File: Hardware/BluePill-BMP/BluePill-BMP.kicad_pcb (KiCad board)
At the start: 2 copper layers, 70 x 60 mm, 18 parts, among them J1 SWO, J2 JTAG, J3 GDB_COMM, J4 VCC, J5 GND, J6 LogicAna, U1 FT232RL_Breakout, U2 STM32F103 BluePill

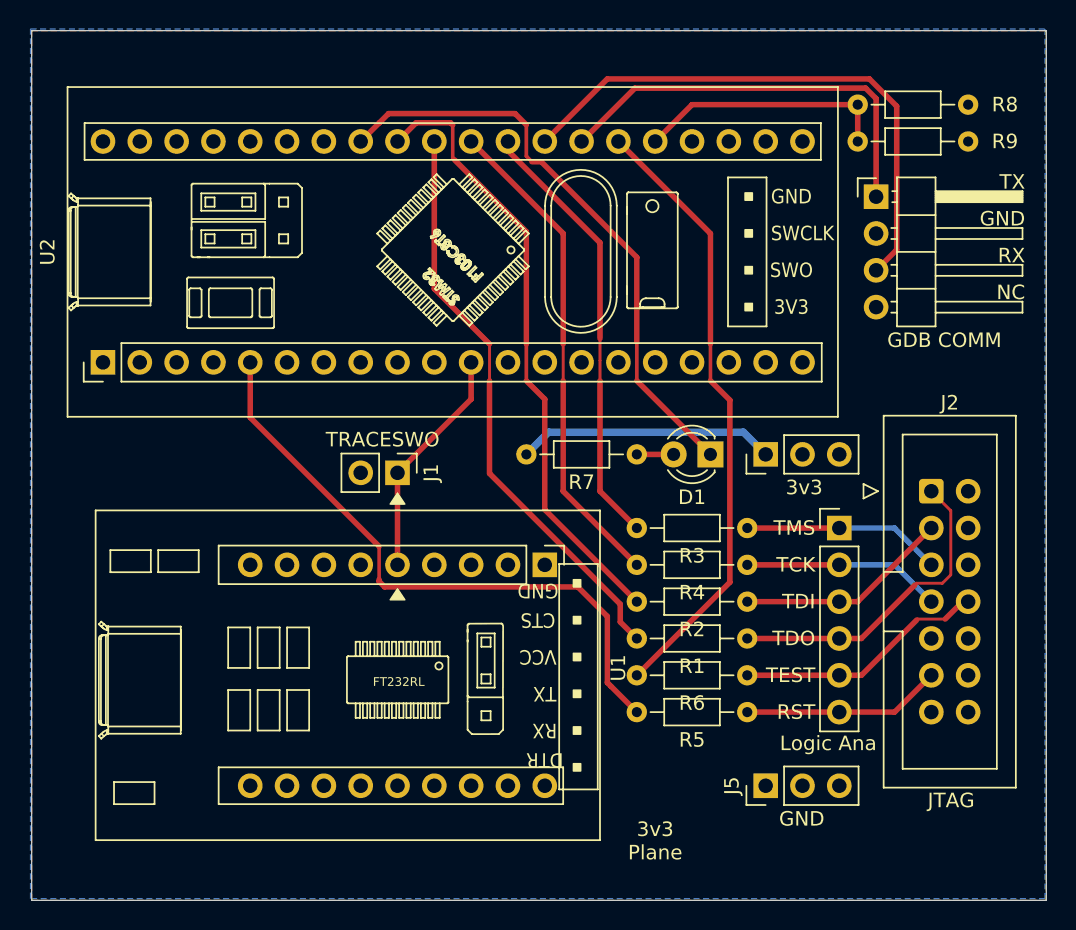
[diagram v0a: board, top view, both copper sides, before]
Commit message: - JTAG over SPI
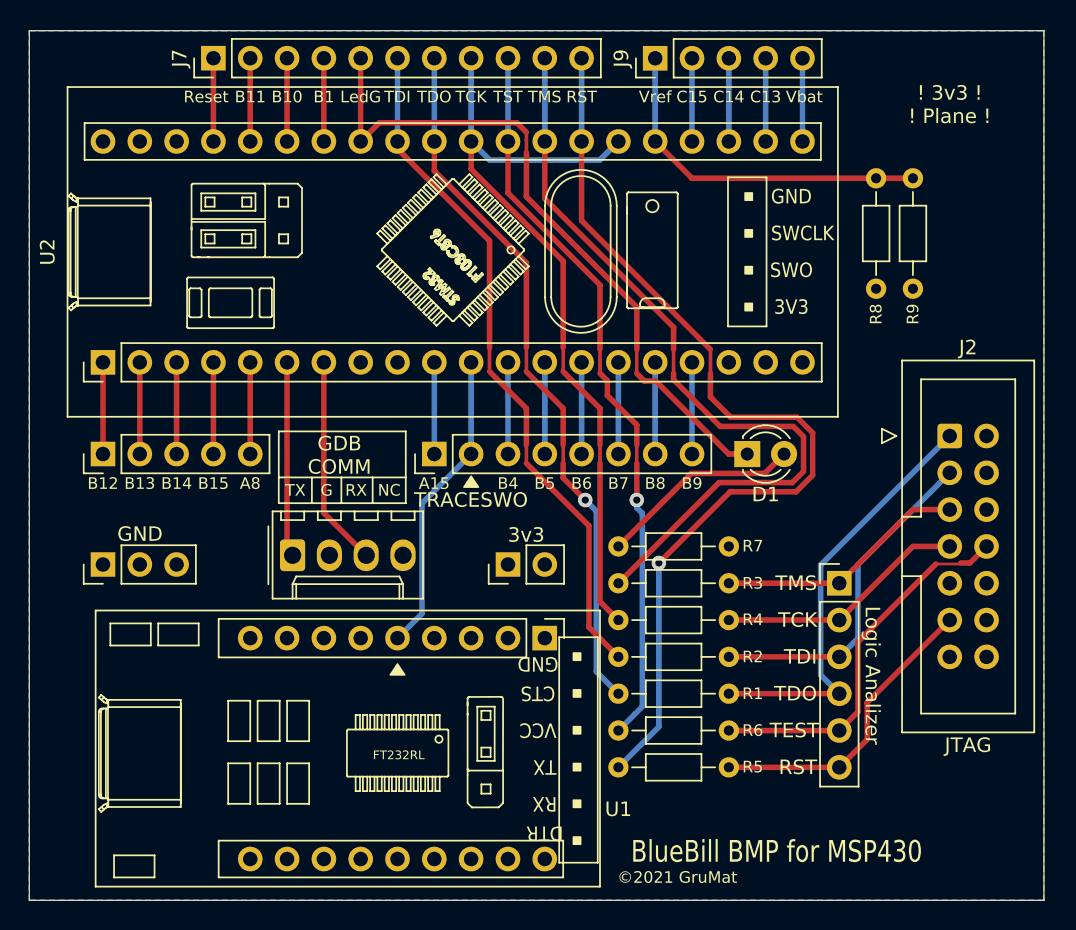
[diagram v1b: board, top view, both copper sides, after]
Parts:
- added J7: Conn_01x11, Connector_PinHeader_2.54mm:PinHeader_1x11_P2.54mm_Vertical, F.Cu at (129.5, 66.9)
- added J8: Conn_01x05, Connector_PinHeader_2.54mm:PinHeader_1x05_P2.54mm_Vertical, F.Cu at (121.9, 94.2)
- added J9: Conn_01x05, Connector_PinHeader_2.54mm:PinHeader_1x05_P2.54mm_Vertical, F.Cu at (160.0, 66.9)
- J1: value SWO -> Conn_01x08; footprint Connector_PinHeader_2.54mm:PinHeader_1x02_P2.54mm_Vertical -> Connector_PinHeader_2.54mm:PinHeader_1x08_P2.54mm_Vertical
- J3: footprint Connector_PinHeader_2.54mm:PinHeader_1x04_P2.54mm_Horizontal -> Connector_Molex:Molex_KK-254_AE-6410-04A_1x04_P2.54mm_Vertical
- J4: footprint Connector_PinHeader_2.54mm:PinHeader_1x03_P2.54mm_Vertical -> Connector_PinHeader_2.54mm:PinHeader_1x02_P2.54mm_Vertical
- moved J5 48.2 mm to (121.9, 101.8)
- moved J3 47.3 mm to (135.0, 101.2)
- moved J4 19.3 mm to (149.9, 101.8)
- moved R9 10.9 mm to (177.8, 82.8), turned to 90 degrees
- moved R7 6.48 mm to (157.5, 100.6), turned to 0 degrees
- moved R8 5.24 mm to (175.3, 75.2), turned to 270 degrees
- moved U1 5.06 mm to (152.4, 106.9)
- moved J2 4.02 mm to (180.3, 93.0)
- moved R1 4.02 mm to (165.1, 110.7)
- moved R3 4.02 mm to (165.1, 103.1)
- moved R4 4.02 mm to (165.1, 105.7)
- moved R5 4.02 mm to (165.1, 115.8)
- moved R6 4.02 mm to (165.1, 113.3)
- moved R2 4.02 mm to (165.1, 108.2)
- moved J6 3.81 mm to (172.7, 103.1)
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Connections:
- J1 pad 1: /TRACESWO -> /PA15
- J1 pad 2: GND -> /TRACESWO
- U2 pad 1: Net-(U2-Pad1) -> /PB12
- U2 pad 10: Net-(U2-Pad10) -> /PA15
- U2 pad 12: Net-(U2-Pad12) -> /PB4
- U2 pad 13: Net-(U2-Pad13) -> /PB5
- U2 pad 14: Net-(U2-Pad14) -> /PB6
- U2 pad 15: Net-(U2-Pad15) -> /PB7
- U2 pad 16: Net-(U2-Pad16) -> /PB8
- U2 pad 17: Net-(U2-Pad17) -> /PB9
- U2 pad 2: Net-(U2-Pad2) -> /PB13
- U2 pad 21: Net-(U2-Pad21) -> /VBAT
- U2 pad 22: Net-(U2-Pad22) -> /PC13
- U2 pad 23: Net-(U2-Pad23) -> /PC14
- U2 pad 24: Net-(U2-Pad24) -> /PC15
- U2 pad 26: /BTEST -> /BTCK
- U2 pad 27: /GDB_TX -> /BRST
- U2 pad 28: /GDB_RX -> /BTMS
- U2 pad 29: /BTMS -> /BTEST
- U2 pad 3: Net-(U2-Pad3) -> /PB14
- U2 pad 34: Net-(U2-Pad34) -> /PB1
- U2 pad 35: Net-(U2-Pad35) -> /PB10
- U2 pad 36: Net-(U2-Pad36) -> /PB11
- U2 pad 37: Net-(U2-Pad37) -> /RST
- U2 pad 4: Net-(U2-Pad4) -> /PB15
- U2 pad 5: /BRST -> /PA8
- U2 pad 6: Net-(U2-Pad6) -> /GDB_TX
- U2 pad 7: Net-(U2-Pad7) -> /GDB_RX
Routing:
- net /BTMS: track 30.4 -> 54.8 mm
- net /GDB_RX: track 38.8 -> 14.5 mm
- net /BRST: track 43.0 -> 66.4 mm, vias 0 -> 1
- net /BTCK: track 33.9 -> 54.2 mm
- net +3V3: track 17.8 -> 0.00 mm
- net /GDB_TX: track 28.9 -> 13.5 mm
- net Net-(D1-Pad2): track 2.54 -> 14.1 mm
- net /BTDO: track 40.1 -> 49.1 mm, vias 0 -> 1
- net /JTDI: track 14.8 -> 23.5 mm
- net /JTEST: track 17.3 -> 25.9 mm
- net /BTEST: track 42.7 -> 50.9 mm, vias 0 -> 1
- net /JTDO: track 22.2 -> 29.6 mm
- net /JRST: track 13.8 -> 20.9 mm
- net /VREF: track 17.6 -> 24.6 mm
- net /LEDG: track 40.9 -> 47.7 mm
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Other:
- board text added: "! 3v3 ! ! Plane !"
- board text added: "A15"
- board text added: "A8"
- board text added: "B1"
- board text added: "B10"
- board text added: "B11"
- board text added: "B12"
- board text added: "B13"
- board text added: "B14"
- board text added: "B15"
- board text added: "B4"
- board text added: "B5"
- board text added: "B6"
- board text added: "B7"
- board text added: "B8"
- board text added: "B9"
- board text added: "BlueBill BMP for MSP430"
- board text added: "C13"
- board text added: "C14"
- board text added: "C15"
- board text added: "G"
- board text added: "LedG"
- board text added: "Logic Analizer"
- board text added: "Reset"
- board text added: "TST"
- board text added: "Vbat"
- board text added: "Vref"
- board text added: "©2021 GruMat"
- board text removed: "3v3 Plane"
- board text removed: "Logic Ana"

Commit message: Updated Hardware Schematics and Boards
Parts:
- removed J9: Conn_01x05, Connector_PinHeader_2.54mm:PinHeader_1x05_P2.54mm_Vertical
- removed the R1 at (165.1, 110.7)
- added C1: 100nF, Capacitor_THT:C_Disc_D4.3mm_W1.9mm_P5.00mm, F.Cu at (182.9, 85.3)
- added R10: 330, Resistor_THT:R_Axial_DIN0204_L3.6mm_D1.6mm_P7.62mm_Horizontal, F.Cu at (157.5, 115.8)
- added R11: 330, Resistor_THT:R_Axial_DIN0204_L3.6mm_D1.6mm_P7.62mm_Horizontal, F.Cu at (165.1, 110.7)
- added R9: 330, Resistor_THT:R_Axial_DIN0204_L3.6mm_D1.6mm_P7.62mm_Horizontal, F.Cu at (157.5, 118.3)
- J1: value Conn_01x08 -> Conn_01x07; footprint Connector_PinHeader_2.54mm:PinHeader_1x08_P2.54mm_Vertical -> Connector_PinHeader_2.54mm:PinHeader_1x07_P2.54mm_Vertical
- J3: renamed from J7; footprint Connector_PinHeader_2.54mm:PinHeader_1x11_P2.54mm_Vertical -> Connector_PinHeader_2.54mm:PinHeader_1x13_P2.54mm_Vertical
- J8: renamed from J6; footprint Connector_PinHeader_2.54mm:PinHeader_1x06_P2.54mm_Vertical -> Connector_PinHeader_2.54mm:PinHeader_1x07_P2.54mm_Vertical
- moved J3 33.0 mm to (162.6, 66.9), turned to 270 degrees
- moved R8 5.10 mm to (165.1, 108.2)
- moved R1 2.56 mm to (157.5, 98.0)
- moved R6 2.56 mm to (165.1, 103.1)
- moved R4 2.56 mm to (165.1, 105.6)
- moved R5 2.56 mm to (165.1, 100.6)
- moved R7 2.56 mm to (165.1, 113.3)
- moved J1 2.54 mm to (147.3, 94.2)
- renumbered J8 to J2, J3 to J4, J4 to J5, J5 to J6, J2 to J7, R7 to R1, R8 to R2, R9 to R3, R2 to R4, R3 to R5, R4 to R6, R5 to R7, R6 to R8
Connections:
- J1 pad 1: /PA15 -> /TRACESWO
- J1 pad 2: /TRACESWO -> Net-(J1-Pad2)
- J1 pad 3: /PB4 -> /PB5
- J1 pad 4: /PB5 -> /BTCK
- J1 pad 5: /PB6 -> /BTMS
- J1 pad 6: /PB7 -> /PB8
- J1 pad 7: /PB8 -> /PB9
- J2 pad 1: /PB12 -> /BRST
- J2 pad 2: /PB13 -> /BTCK
- J2 pad 3: /PB14 -> /JTDO
- J2 pad 4: /PB15 -> /BTDI
- J2 pad 5: /PA8 -> /BTEST
- J3 pad 1: /RST -> /PC13
- J3 pad 10: /BTMS -> /LEDG
- J3 pad 11: /BRST -> /PB1
- J3 pad 2: /PB11 -> /VREF
- J3 pad 3: /PB10 -> /PA1
- J3 pad 4: /PB1 -> /PA2
- J3 pad 5: /LEDG -> /PA3
- J3 pad 6: /BTDI -> /PA4
- J3 pad 7: /BTDO -> /PA5
- J3 pad 8: /BTCK -> /PA6
- J3 pad 9: /BTEST -> /PA7
- J7 pad 12: Net-(J2-Pad12) -> /JTXD
- J7 pad 13: Net-(J2-Pad13) -> GND
- J7 pad 14: Net-(J2-Pad14) -> /JRXD
- U2 pad 1: /PB12 -> /BRST
- U2 pad 10: /PA15 -> Net-(U2-Pad10)
- U2 pad 12: /PB4 -> Net-(U2-Pad12)
- U2 pad 14: /PB6 -> /BTCK
- U2 pad 15: /PB7 -> /BTMS
- U2 pad 2: /PB13 -> /BTCK
- U2 pad 21: /VBAT -> Net-(U2-Pad21)
- U2 pad 23: /PC14 -> Net-(U2-Pad23)
- U2 pad 24: /PC15 -> Net-(U2-Pad24)
- U2 pad 26: /BTCK -> /PA1
- U2 pad 27: /BRST -> /PA2
- U2 pad 28: /BTMS -> /PA3
- U2 pad 29: /BTEST -> /PA4
- U2 pad 3: /PB14 -> /JTDO
- U2 pad 30: /BTCK -> /PA5
- U2 pad 31: /BTDO -> /PA6
- U2 pad 32: /BTDI -> /PA7
- U2 pad 35: /PB10 -> /BTXD
- U2 pad 36: /PB11 -> /BRXD
- U2 pad 37: /RST -> Net-(U2-Pad37)
- U2 pad 4: /PB15 -> /BTDI
- U2 pad 5: /PA8 -> /BTEST
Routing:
- net +3V3: track 0.00 -> 112.2 mm
- net /BRXD: track 0.00 -> 98.9 mm
- net /BTXD: track 0.00 -> 94.2 mm
- net /JTDO: track 29.6 -> 89.7 mm
- net /BTDO: track 49.1 -> 0.00 mm, vias 1 -> 0
- net /BTMS: track 54.8 -> 15.2 mm
- net /JTXD: track 0.00 -> 31.7 mm
- net /JRXD: track 0.00 -> 27.5 mm
- net /BRST: track 66.4 -> 56.7 mm, vias 1 -> 0
- net /BTDI: track 47.6 -> 55.9 mm
- net /PA6: track 0.00 -> 7.32 mm
- net /PA5: track 0.00 -> 7.32 mm
- net /PA3: track 0.00 -> 7.32 mm
- net /PA2: track 0.00 -> 7.32 mm
- net GND: track 0.00 -> 6.95 mm, vias 0 -> 14
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- added copper zone on F.Cu, net GND
- removed copper zone on F.Cu, net +3V3
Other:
- board text added: "A1"
- board text added: "A2"
- board text added: "A3"
- board text added: "A4"
- board text added: "A5"
- board text added: "A6"
- board text added: "A7"
- board text added: "BRX"
- board text added: "BTX"
- board text added: "JTAG MSP430"
- board text added: "©2021 by GruMat github.com/grumat/black-magic-probe-msp430"
- board text removed: "! 3v3 ! ! Plane !"
- board text removed: "A15"
- board text removed: "A8"
- board text removed: "B10"
- board text removed: "B11"
- board text removed: "B12"
- board text removed: "B13"
- board text removed: "B14"
- board text removed: "B15"
- board text removed: "B4"
- board text removed: "B6"
- board text removed: "B7"
- board text removed: "C14"
- board text removed: "C15"
- board text removed: "JTAG"
- board text removed: "Reset"
- board text removed: "Vbat"
- board text removed: "©2021 GruMat"

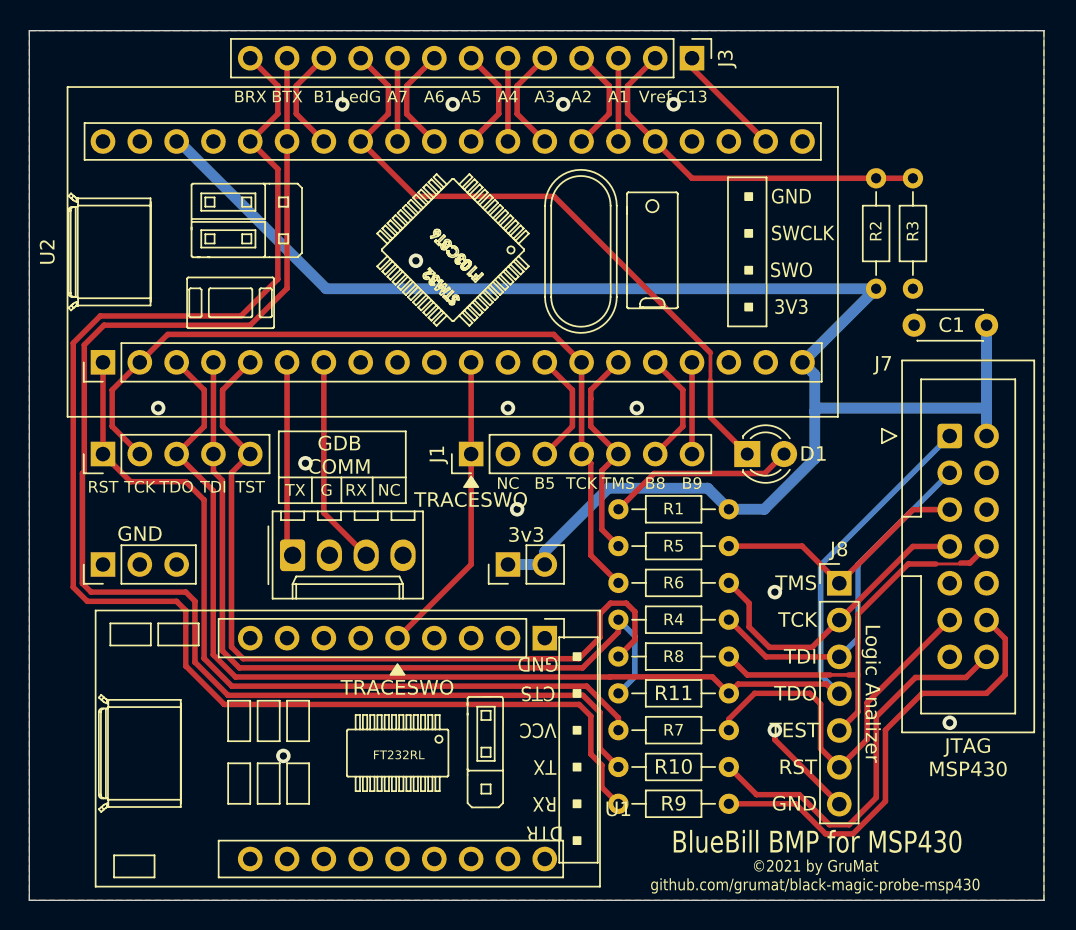
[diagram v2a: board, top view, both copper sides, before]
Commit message: Revised BluePill Prototype board
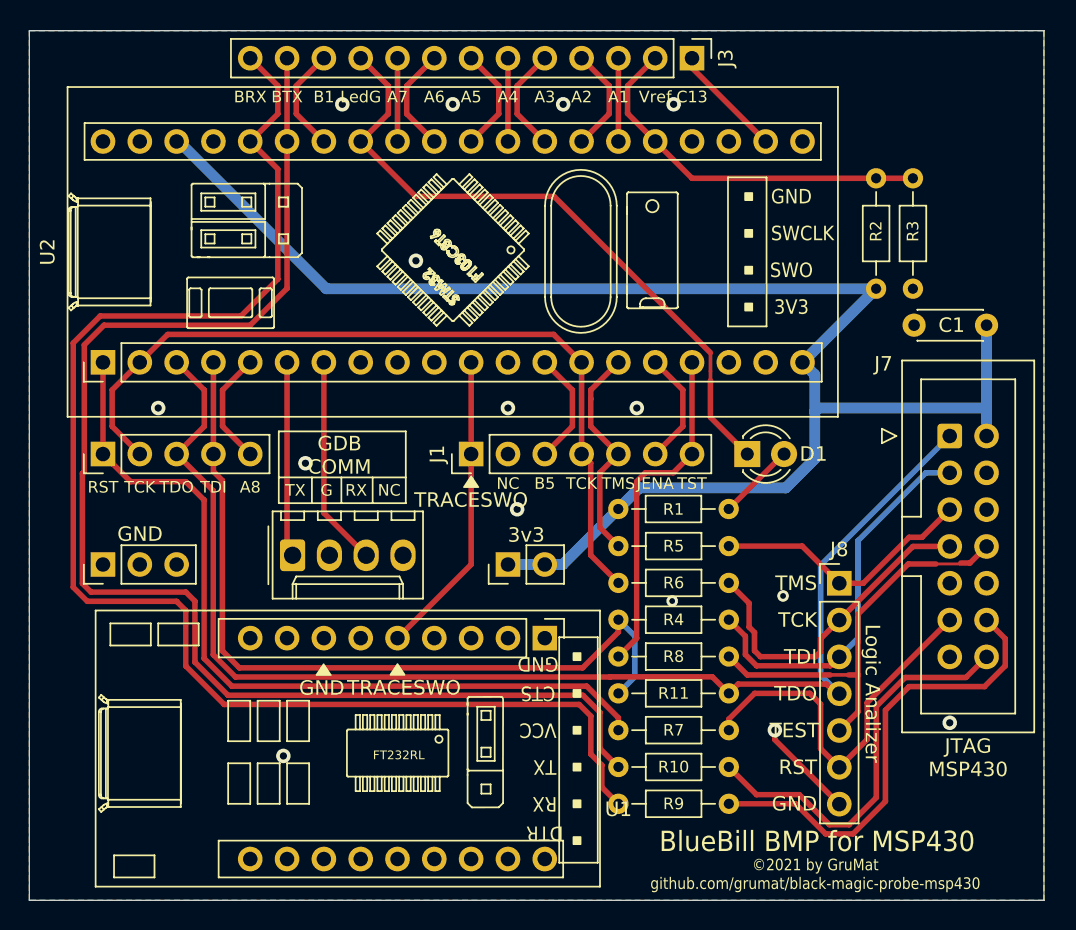
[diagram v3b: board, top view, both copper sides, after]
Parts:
- moved R1 7.61 mm to (165.1, 98.0), turned to 180 degrees
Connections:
- net /PB8 renamed /JENA
- J1 pad 7: /PB9 -> /BTEST
- J2 pad 5: /BTEST -> /PA8
- U2 pad 17: /PB9 -> /BTEST
- U2 pad 5: /BTEST -> /PA8
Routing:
- net /BTEST: track 56.3 -> 23.5 mm
- net /PA8: track 0.00 -> 7.91 mm
- net Net-(D1-Pad2): track 13.0 -> 5.39 mm
- net /PB9: track 6.33 -> 0.00 mm
- net /JTDI: track 24.5 -> 26.8 mm
- net /JTCK: track 20.9 -> 22.7 mm
- net +3V3: track 112.2 -> 110.4 mm
- net GND: vias 14 -> 15
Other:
- board text added: "A8"
- board text added: "JENA"
- board text removed: "B8"
- board text removed: "B9"

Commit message: KiCad6 evaluation
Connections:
- J1 pad 2: Net-(J1-Pad2) -> unconnected-(J1-Pad2)
- J4 pad 4: Net-(J4-Pad4) -> unconnected-(J4-Pad4)
- J7 pad 10: Net-(J7-Pad10) -> unconnected-(J7-Pad10)
- J7 pad 4: Net-(J7-Pad4) -> unconnected-(J7-Pad4)
- J7 pad 6: Net-(J7-Pad6) -> unconnected-(J7-Pad6)
- U1 pad 1: Net-(U1-Pad1) -> unconnected-(U1-Pad1)
- U1 pad 10: Net-(U1-Pad10) -> unconnected-(U1-Pad10)
- U1 pad 11: Net-(U1-Pad11) -> unconnected-(U1-Pad11)
- U1 pad 12: Net-(U1-Pad12) -> unconnected-(U1-Pad12)
- U1 pad 13: Net-(U1-Pad13) -> unconnected-(U1-Pad13)
- U1 pad 14: Net-(U1-Pad14) -> unconnected-(U1-Pad14)
- U1 pad 15: Net-(U1-Pad15) -> unconnected-(U1-Pad15)
- U1 pad 16: Net-(U1-Pad16) -> unconnected-(U1-Pad16)
- U1 pad 17: Net-(U1-Pad17) -> unconnected-(U1-Pad17)
- U1 pad 18: Net-(U1-Pad18) -> unconnected-(U1-Pad18)
- U1 pad 2: Net-(U1-Pad2) -> unconnected-(U1-Pad2)
- U1 pad 3: Net-(U1-Pad3) -> unconnected-(U1-Pad3)
- U1 pad 4: Net-(U1-Pad4) -> unconnected-(U1-Pad4)
- U1 pad 6: Net-(U1-Pad6) -> unconnected-(U1-Pad6)
- U1 pad 8: Net-(U1-Pad8) -> unconnected-(U1-Pad8)
- U1 pad 9: Net-(U1-Pad9) -> unconnected-(U1-Pad9)
- U2 pad 10: Net-(U2-Pad10) -> unconnected-(U2-Pad10)
- U2 pad 12: Net-(U2-Pad12) -> unconnected-(U2-Pad12)
- U2 pad 18: Net-(U2-Pad18) -> unconnected-(U2-Pad18)
- U2 pad 21: Net-(U2-Pad21) -> unconnected-(U2-Pad21)
- U2 pad 23: Net-(U2-Pad23) -> unconnected-(U2-Pad23)
- U2 pad 24: Net-(U2-Pad24) -> unconnected-(U2-Pad24)
- U2 pad 37: Net-(U2-Pad37) -> unconnected-(U2-Pad37)
- U2 pad 8: Net-(U2-Pad8) -> unconnected-(U2-Pad8)
- U2 pad 9: Net-(U2-Pad9) -> unconnected-(U2-Pad9)
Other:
- net class Default removed
- net class Power removed
